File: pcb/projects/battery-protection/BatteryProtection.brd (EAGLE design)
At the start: 76.2 x 25.4 mm, 14 parts, among them U1 BQ29700DSET

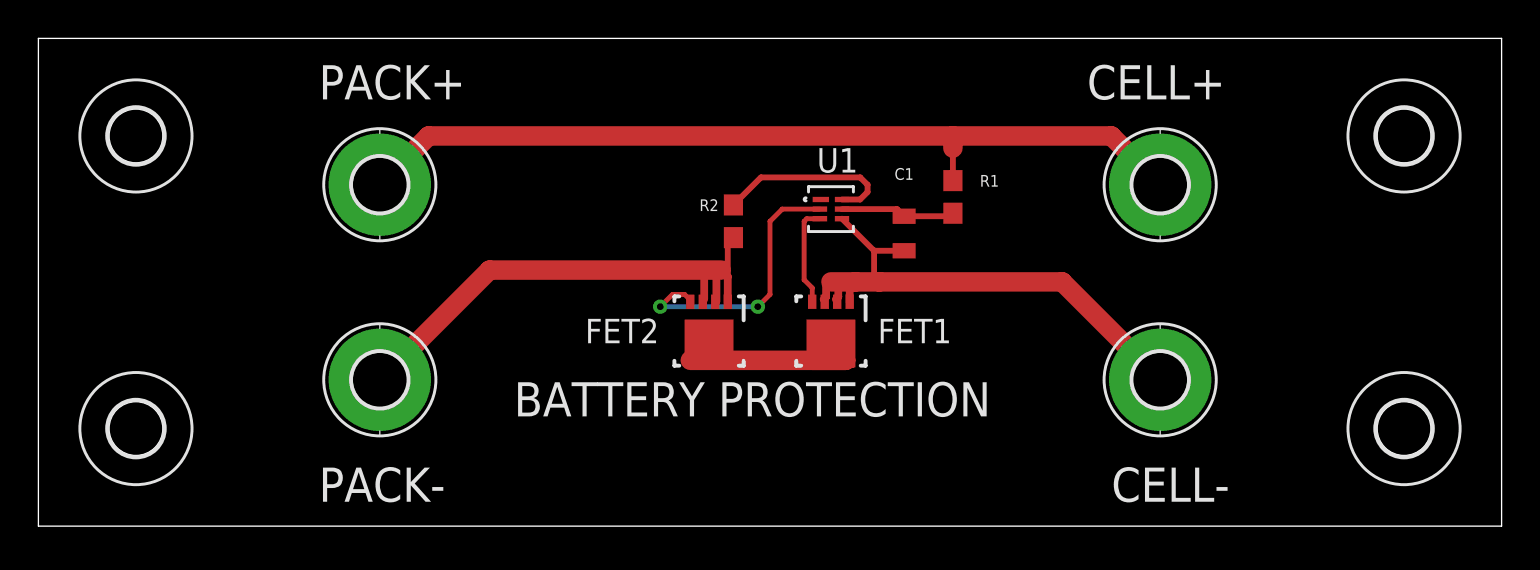
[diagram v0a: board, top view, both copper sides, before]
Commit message: v1.1 update
Updates to the flight computer:
* update to max31856 tc to digital to support k/j type tc as well as 7
other types
* add pins for iridium sbd message ready and iridium actively
transmitting
* add capacity sense header
* add through hole connection for battery
* remove rs232 level converter - all pins are 5v tolerant on teensy 3.5
and the iridium operates from 3.5-5.5v DC so no need for it
* add imu orientation silk screen as well as arduino pin map silk on
back
* more meaningful LED names
* added end-to-end activation and battery protection schematic

Other updates
* documentation tex file is now local
* add battery protection schematic, board and gerbers as well as renders
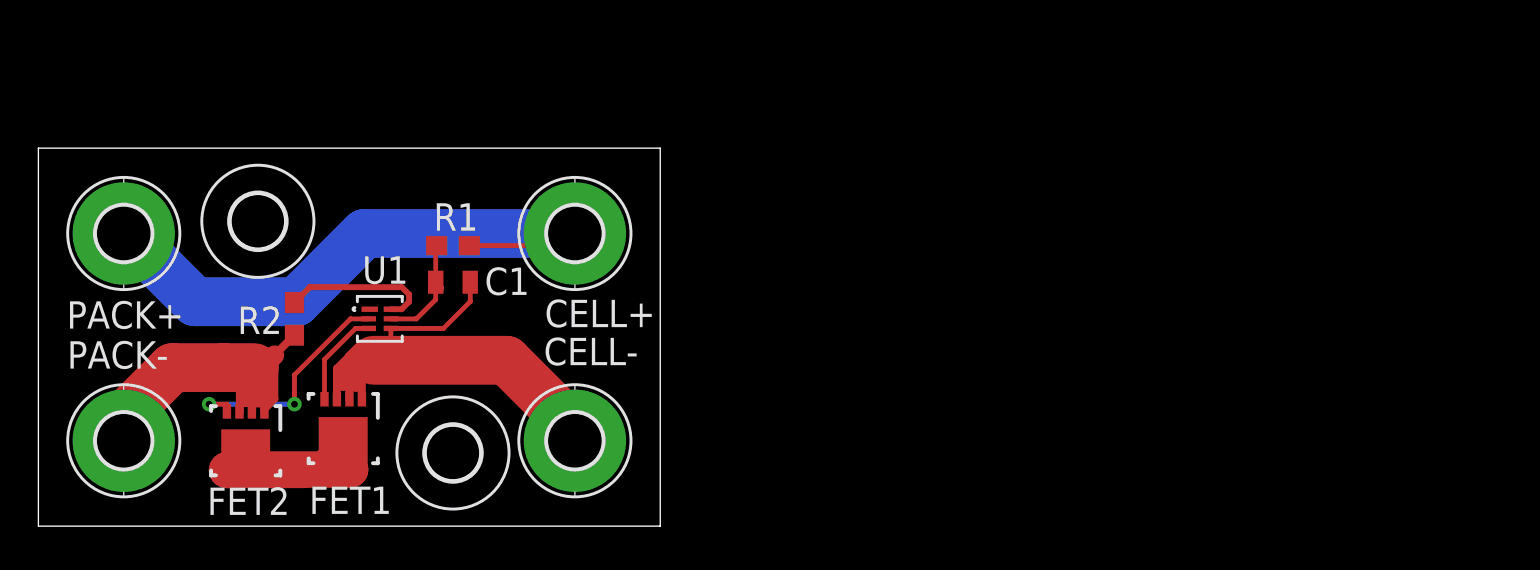
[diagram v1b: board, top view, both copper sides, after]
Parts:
- removed H1, H4: MOUNT-HOLE2.8, holes:2,8
- moved H3 52.2 mm to (21.6, 3.81)
- moved CELL- 30.6 mm to (27.9, 4.45)
- moved CELL+ 30.6 mm to (27.9, 15.2)
- moved R1 26.2 mm to (21.6, 14.6), turned to 0 degrees
- moved FET1 25.9 mm to (15.9, 5.08)
- moved FET2 24.8 mm to (10.8, 4.45)
- moved U1 24.2 mm to (17.8, 10.8)
- moved C1 23.6 mm to (21.6, 12.7), turned to 0 degrees
- moved R2 23.4 mm to (13.3, 10.8)
- moved PACK- 13.7 mm to (4.45, 4.45)
- moved PACK+ 13.6 mm to (4.45, 15.2)
- moved H2 7.75 mm to (11.4, 15.9)
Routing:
- net N$7: track 45.1 -> 32.2 mm
- net N$8: track 24.1 -> 15.1 mm
- net N$3: track 26.1 -> 22.6 mm
- net N$13: track 0.00 -> 2.80 mm
- net N$14: track 0.00 -> 2.57 mm
- net N$2: track 14.7 -> 12.4 mm
- net N$4: track 9.82 -> 12.1 mm
- net N$6: track 9.61 -> 7.95 mm
- net N$12: track 1.07 -> 0.42 mm
- net N$16: track 0.00 -> 0.61 mm
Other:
- board size 76.2 x 25.4 mm -> 32.4 x 19.7 mm
- board text added: "Andrew Perry Matt Ruffner"
- board text added: "KREPE Capsule 2020 Battery Protection Test Board"
- board text removed: "BATTERY PROTECTION"
